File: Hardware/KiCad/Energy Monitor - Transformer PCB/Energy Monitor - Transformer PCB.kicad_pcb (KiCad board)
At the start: 2 copper layers, 100 x 100 mm, 25 parts, among them J1 Conn_01x02, J10 Conn_02x05_Odd_Even, J2 Conn_01x02, J3 Conn_01x02, J4 Conn_02x05_Odd_Even, J5 Conn_02x05_Odd_Even, J6 Conn_02x05_Odd_Even, J7 Conn_02x05_Odd_Even, J8 Conn_02x05_Odd_Even, J9 Conn_02x05_Odd_Even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

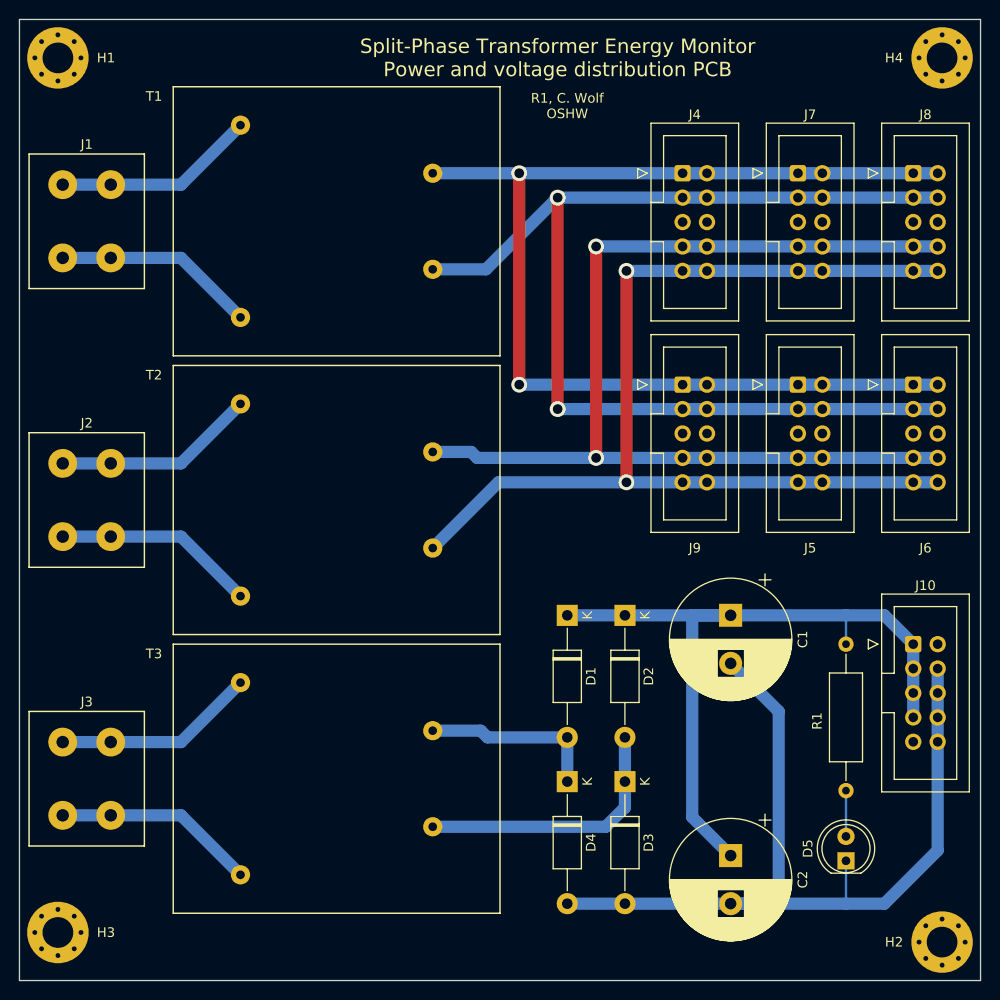
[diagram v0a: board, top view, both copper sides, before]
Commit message: This seems to be getting progressively more complicated. Library cleanup, moved everything to my system library.
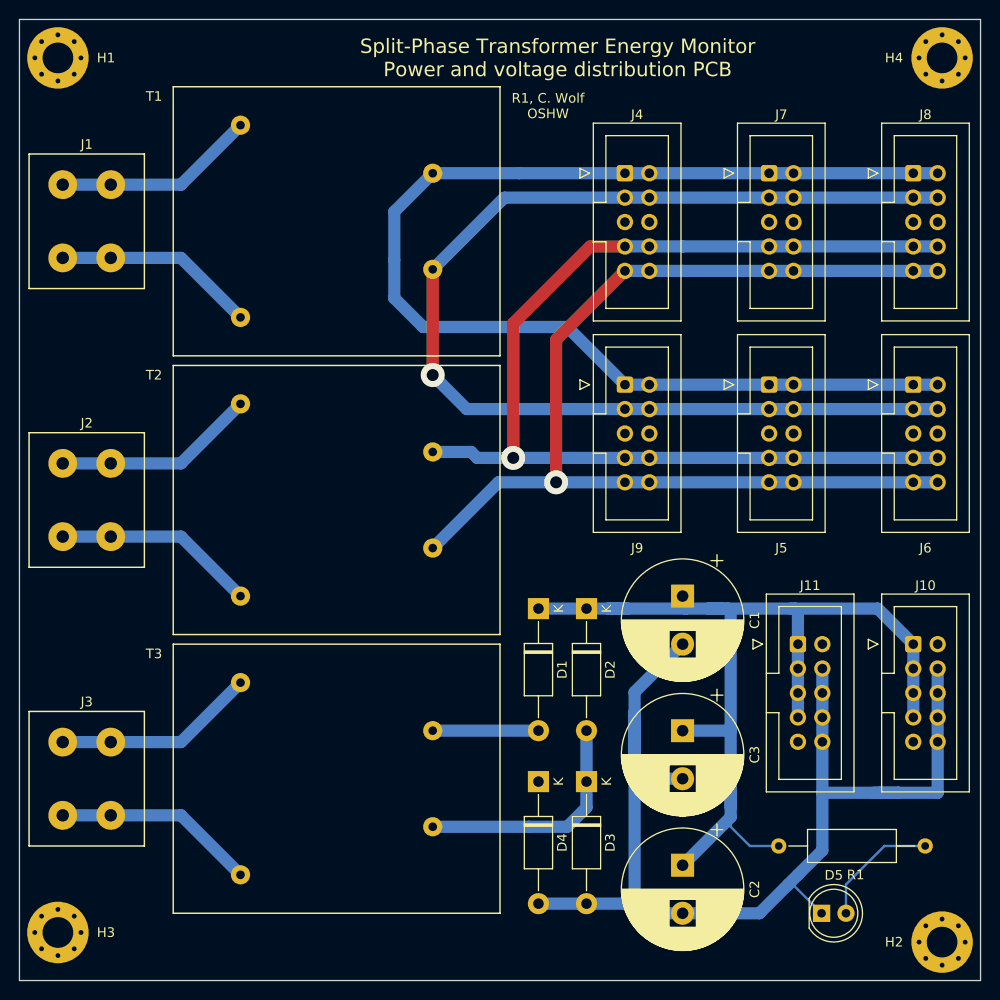
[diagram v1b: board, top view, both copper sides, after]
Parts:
- added C3: CP1, Capacitor_THT:CP_Radial_D12.5mm_P5.00mm, F.Cu at (119.0, 124.0)
- added J11: Conn_02x05_Odd_Even, Connector_IDC:IDC-Header_2x05_P2.54mm_Vertical, F.Cu at (131.0, 115.0)
- moved R1 22.1 mm to (129.0, 136.0), turned to 0 degrees
- moved D5 6.02 mm to (133.5, 143.0), turned to 0 degrees
- moved J4 6.00 mm to (113.0, 66.0)
- moved J9 6.00 mm to (113.0, 88.0)
- moved C1 5.39 mm to (119.0, 110.0)
- moved C2 5.10 mm to (119.0, 138.0)
- moved D2 4.06 mm to (109.0, 111.3)
- moved D3 4.00 mm to (109.0, 129.3)
- moved D1 3.08 mm to (104.0, 111.3)
- moved D4 3.00 mm to (104.0, 129.3)
- moved J5 3.00 mm to (128.0, 88.0)
- moved J7 3.00 mm to (128.0, 66.0)
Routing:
- net +9V: track 78.5 -> 109.3 mm
- net GND: track 96.4 -> 124.9 mm
- net Net-(J4-Pad1): track 118.1 -> 127.5 mm, vias 2 -> 0
- net Net-(D5-Pad2): track 4.76 -> 12.9 mm
- net Net-(D1-Pad2): track 18.9 -> 11.0 mm
- net Net-(J4-Pad7): track 110.3 -> 114.3 mm, vias 2 -> 1
- net Net-(J4-Pad3): track 117.2 -> 120.6 mm, vias 2 -> 1
- net Net-(D2-Pad2): track 28.1 -> 24.8 mm
- net Net-(J4-Pad10): track 109.8 -> 112.7 mm, vias 2 -> 1

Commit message: MOAR.
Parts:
- added REF**: OSHW-LOGOS, custom:OSHW-LOGO-S, F.Cu at (105.5, 61.5)
- T3: value EI30-15.5 -> AHI050; footprint Energy Monitor - Transformer PCB:EI30-15.5-TH -> custom:AHI050-TH
- moved T1 6.58 mm to (84.0, 64.5)
- moved T2 6.58 mm to (84.0, 93.5)
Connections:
- T3 pad 5: Net-(J3-Pad2) -> Net-(D2-Pad2)
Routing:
- net Net-(J3-Pad1): track 21.1 -> 44.2 mm
- net Net-(D2-Pad2): track 24.8 -> 44.5 mm
- net Net-(J4-Pad1): track 127.5 -> 147.1 mm
- net Net-(D1-Pad2): track 11.0 -> 29.6 mm
- net Net-(J1-Pad2): track 21.1 -> 31.9 mm
- net Net-(J3-Pad2): track 21.1 -> 31.9 mm
- net Net-(J2-Pad2): track 21.1 -> 26.9 mm
- net Net-(J2-Pad1): track 21.1 -> 26.5 mm
- net Net-(J1-Pad1): track 21.1 -> 26.2 mm
- net Net-(J4-Pad3): track 120.6 -> 125.7 mm
- net Net-(J4-Pad7): track 114.3 -> 116.0 mm
- net GND: track 124.9 -> 123.5 mm
- net Net-(J4-Pad10): track 112.7 -> 111.8 mm
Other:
- board text added: "R1, C. Wolf"
- board text removed: "R1, C. Wolf OSHW"
